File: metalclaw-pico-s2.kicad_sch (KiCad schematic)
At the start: 62 parts, among them J1 USB_C_Receptacle_USB2.0_14P, J2 Conn_01x05, J3 Conn_02x05_Odd_Even, U1 ESP32-S2, U2 MX25L3236FM2I-08G-TR, U3 APS6404L-3SQRx-SN, U5 XC6220B331MR, Y1 XRCGB40M000F1S2FR0

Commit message: Rearrange pins to fit Pi Pico layout
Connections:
- net GP0: now also U1.13 (GPIO8); no longer U1.6 (GPIO1)
- net GP1: now also U1.14 (GPIO9); no longer U1.7 (GPIO2)
- net GP10: now also U1.38 (GPIO34); no longer U1.16 (GPIO11)
- net GP11: now also U1.39 (GPIO35); no longer U1.17 (GPIO12)
- net GP12: now also U1.40 (GPIO36); no longer U1.18 (GPIO13)
- net GP13: now also U1.42 (GPIO38); no longer U1.19 (GPIO14)
- net GP14: now also U1.41 (GPIO37); no longer U1.21 (XTAL_32K_P)
- net GP15: now also R31.2, U1.55 (GPIO46); no longer U1.22 (XTAL_32K_N)
- net GP16: now also U1.6 (GPIO1); no longer U1.37 (GPIO33)
- net GP17: now also U1.7 (GPIO2); no longer U1.38 (GPIO34)
- net GP18: now also U1.8 (GPIO3); no longer U1.39 (GPIO35)
- net GP19: now also U1.9 (GPIO4); no longer U1.40 (GPIO36)
- net GP2: now also U1.15 (GPIO10); no longer U1.8 (GPIO3)
- net GP20: now also U1.10 (GPIO5); no longer U1.42 (GPIO38)
- net GP21: now also U1.11 (GPIO6); no longer U1.41 (GPIO37)
- net GP22: now also U1.12 (GPIO7); no longer R31.2, U1.55 (GPIO46)
- net GP3: now also U1.16 (GPIO11); no longer U1.9 (GPIO4)
- net GP4: now also U1.17 (GPIO12); no longer U1.10 (GPIO5)
- net GP5: now also U1.18 (GPIO13); no longer U1.11 (GPIO6)
- net GP6: now also U1.19 (GPIO14); no longer U1.12 (GPIO7)
- net GP7: now also U1.21 (XTAL_32K_P); no longer U1.13 (GPIO8)
- net GP8: now also U1.22 (XTAL_32K_N); no longer U1.14 (GPIO9)
- net GP9: now also U1.37 (GPIO33); no longer U1.15 (GPIO10)
- no-connect marks 3 -> 4
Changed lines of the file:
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@@
 	)
 	(no_connect
+		(at 111.76 85.09)
+	)
+	(no_connect
 		(at 166.37 46.99)
 	)
@@
 	)
 	(label "GP5"
-		(at 71.12 147.32 90)
+		(at 88.9 147.32 90)
 		(effects
 			(font
@@
 	)
 	(label "GP7"
-		(at 76.2 147.32 90)
+		(at 114.3 153.67 90)
 		(effects
 			(font
@@
 	)
 	(label "GP22"
-		(at 109.22 66.04 270)
+		(at 73.66 147.32 90)
 		(effects
 			(font
 				(size 1.27 1.27)
 			)
-			(justify right bottom)
+			(justify left bottom)
 		)
 	)
@@
 	)
 	(label "GP6"
-		(at 73.66 147.32 90)
+		(at 91.44 147.32 90)
 		(effects
 			(font
@@
 	)
 	(label "GP14"
-		(at 114.3 153.67 90)
+		(at 88.9 66.04 270)
 		(effects
 			(font
 				(size 1.27 1.27)
 			)
-			(justify left bottom)
+			(justify right bottom)
 		)
 	)
 	(label "GP20"
-		(at 86.36 66.04 270)
+		(at 68.58 147.32 90)
 		(effects
 			(font
 				(size 1.27 1.27)
 			)
-			(justify right bottom)
+			(justify left bottom)
 		)
 	)
 	(label "GP19"
-		(at 83.82 66.04 270)
+		(at 66.04 147.32 90)
 		(effects
 			(font
 				(size 1.27 1.27)
 			)
-			(justify right bottom)
+			(justify left bottom)
 		)
 	)
 	(label "GP13"
-		(at 91.44 147.32 90)
+		(at 86.36 66.04 270)
 		(effects
 			(font
 				(size 1.27 1.27)
 			)
-			(justify left bottom)
+			(justify right bottom)
 		)
 	)
 	(label "GP15"
-		(at 116.84 153.67 90)
+		(at 109.22 66.04 270)
 		(effects
 			(font
 				(size 1.27 1.27)
 			)
-			(justify left bottom)
+			(justify right bottom)
 		)
 	)
 	(label "GP17"
-		(at 78.74 66.04 270)
+		(at 60.96 147.32 90)
 		(effects
 			(font
 				(size 1.27 1.27)
 			)
-			(justify right bottom)
+			(justify left bottom)
 		)
 	)
@@
 	)
 	(label "GP2"
-		(at 63.5 147.32 90)
+		(at 81.28 147.32 90)
 		(effects
 			(font
@@
 	)
 	(label "GP1"
-		(at 60.96 147.32 90)
+		(at 78.74 147.32 90)
 		(effects
 			(font
@@
 	)
 	(label "GP8"
-		(at 78.74 147.32 90)
+		(at 116.84 153.67 90)
 		(effects
 			(font
@@
 	)
 	(label "GP3"
-		(at 66.04 147.32 90)
+		(at 83.82 147.32 90)
 		(effects
 			(font
@@
 	)
 	(label "GP18"
-		(at 81.28 66.04 270)
+		(at 63.5 147.32 90)
 		(effects
 			(font
 				(size 1.27 1.27)
 			)
-			(justify right bottom)
+			(justify left bottom)
 		)
 	)
 	(label "GP21"
-		(at 88.9 66.04 270)
+		(at 71.12 147.32 90)
 		(effects
 			(font
 				(size 1.27 1.27)
 			)
-			(justify right bottom)
+			(justify left bottom)
 		)
 	)
 	(label "GP11"
-		(at 86.36 147.32 90)
+		(at 81.28 66.04 270)
 		(effects
 			(font
 				(size 1.27 1.27)
 			)
-			(justify left bottom)
+			(justify right bottom)
 		)
 	)
@@
 	)
 	(label "GP9"
-		(at 81.28 147.32 90)
+		(at 76.2 66.04 270)
 		(effects
 			(font
 				(size 1.27 1.27)
 			)
-			(justify left bottom)
+			(justify right bottom)
 		)
 	)
 	(label "GP10"
-		(at 83.82 147.32 90)
+		(at 78.74 66.04 270)
 		(effects
 			(font
 				(size 1.27 1.27)
 			)
-			(justify left bottom)
+			(justify right bottom)
 		)
 	)
@@
 	)
 	(label "GP16"
-		(at 76.2 66.04 270)
+		(at 58.42 147.32 90)
 		(effects
 			(font
 				(size 1.27 1.27)
 			)
-			(justify right bottom)
+			(justify left bottom)
 		)
 	)
@@
 	)
 	(label "GP0"
-		(at 58.42 147.32 90)
+		(at 76.2 147.32 90)
 		(effects
 			(font
@@
 	)
 	(label "GP4"
-		(at 68.58 147.32 90)
+		(at 86.36 147.32 90)
 		(effects
 			(font
@@
 	)
 	(label "GP12"
-		(at 88.9 147.32 90)
+		(at 83.82 66.04 270)
 		(effects
 			(font
 				(size 1.27 1.27)
 			)
-			(justify left bottom)
+			(justify right bottom)
 		)
 	)

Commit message: Add initial Pi Pico footprint
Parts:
- A2: footprint Module:RaspberryPi_Pico_SMD_HandSolder -> MetalClaw:RaspberryPi_Pico_SMD
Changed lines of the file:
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@@
 			)
 		)
-		(property "Footprint" "Module:RaspberryPi_Pico_SMD_HandSolder"
+		(property "Footprint" "MetalClaw:RaspberryPi_Pico_SMD"
 			(at 209.55 161.29 0)
 			(effects

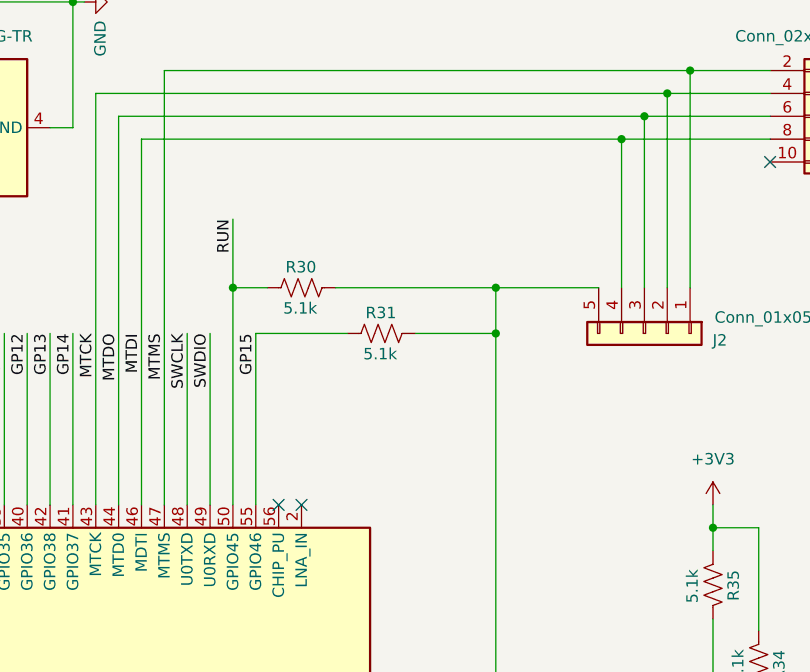
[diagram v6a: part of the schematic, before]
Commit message: Add pull-up on CHIP_PU
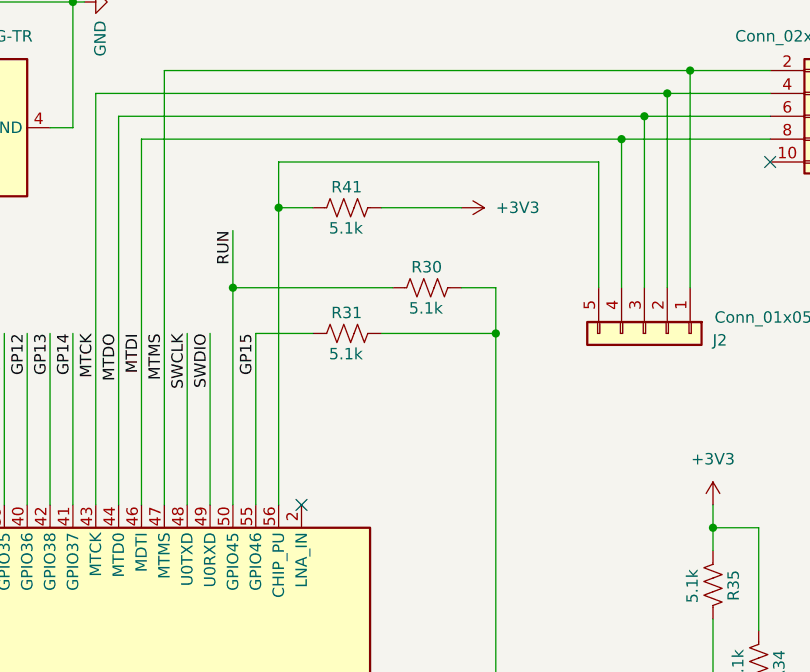
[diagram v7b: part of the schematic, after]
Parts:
- added R41: 5.1k, Resistor_SMD:R_0402_1005Metric, symbol Device:R_US
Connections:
- net +3V3: now also R41.1
- net GND: no longer J2.5 (Pin_5)
- net at U1.56 (CHIP_PU): now also J2.5 (Pin_5), R41.2
- no-connect marks 4 -> 3
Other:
- moved on the sheet: R30, R31

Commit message: Refine schematic and layout more
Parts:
- added C12, C13: C, Capacitor_SMD:C_0402_1005Metric, symbol Device:C
- added C16, C17: 100n, Capacitor_SMD:C_0402_1005Metric, symbol Device:C
- added D1: D_Schottky, symbol Device:D_Schottky
- added J4: Conn_Coaxial, Connector_Coaxial:U.FL_Hirose_U.FL-R-SMT-1_Vertical, symbol Connector:Conn_Coaxial
- added L1: L, Inductor_SMD:L_0402_1005Metric, symbol Device:L
- added R42: 5.1k, Resistor_SMD:R_0402_1005Metric, symbol Device:R_US
- added SW1, SW2: SW_Push, Button_Switch_SMD:SW_Push_SPST_NO_Alps_SKRK, symbol Switch:SW_Push
- J2: now not fitted
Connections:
- net GP15 is gone; now on net GP14: R27.2, R31.2, R40.2, U1.55 (GPIO46)
- net GP7 is gone; now on net GP6: R17.2, R19.2, U1.21 (XTAL_32K_P)
- net +3V3: now also R42.1
- net 3V3_EN: now also R41.2, C16.2
- net GND: now also C12.2, C13.2, J4.2 (Ext), SW1.1, SW2.1
- net VBUS: now also D1.2 (A); no longer C1.1, U5.1 (VIN), U5.3 (CE)
- net VS: now also C1.1, U5.1 (VIN), U5.3 (CE), D1.1 (K)
- net RESET: now reaches J2.5 (Pin_5), U1.56 (CHIP_PU)
- net RESET: now also C17.2, R42.2; no longer R41.2
- net at U1.2 (LNA_IN): now also C12.1, L1.1
- new net: C13.1, J4.1 (In), L1.2
- new net: C17.1, SW1.2
- new net: C16.1, SW2.2
- no-connect marks 3 -> 2
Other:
- moved on the sheet: A2, C1, C3, J3, R17, R30, R31, R32, R33, R34, R35, R36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
